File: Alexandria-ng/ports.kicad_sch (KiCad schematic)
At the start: 56 parts, among them J1 Eth0, J10 PoE3, J11 PoE4, J12 FFC, J2 Eth1, J3 Eth2, J4 Eth3, J5 Eth4, J6 SFP+, J7 PoE0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

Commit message: Update to KiCad 7.0, add footprint to RJ45 jacks
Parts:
- J1, J2, J3, J4, J5: footprint (none) -> Connector_RJ:RJ45_Amphenol_RJHSE538X
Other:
- note added: "DS1128: Footprint matches Amphenol RJHSE538X"

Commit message: Annotate & assign footprints
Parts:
- D3, D4, D5: footprint (none) -> LED_SMD:LED_0603_1608Metric_Pad1.05x0.95mm_HandSolder
- J6: footprint (none) -> Connector:Connector_SFP_and_Cage
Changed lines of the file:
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@@
       (effects (font (size 1.27 1.27)) (justify right))
     )
-    (property "Footprint" "" (at 217.17 41.91 0)
+    (property "Footprint" "LED_SMD:LED_0603_1608Metric_Pad1.05x0.95mm_HandSolder" (at 217.17 41.91 0)
       (effects (font (size 1.27 1.27)) hide)
     )
@@
       (effects (font (size 1.27 1.27)) (justify right))
     )
-    (property "Footprint" "" (at 271.78 35.56 0)
+    (property "Footprint" "LED_SMD:LED_0603_1608Metric_Pad1.05x0.95mm_HandSolder" (at 271.78 35.56 0)
       (effects (font (size 1.27 1.27)) hide)
     )
@@
       (effects (font (size 1.27 1.27)) (justify right))
     )
-    (property "Footprint" "" (at 278.13 53.34 0)
+    (property "Footprint" "LED_SMD:LED_0603_1608Metric_Pad1.05x0.95mm_HandSolder" (at 278.13 53.34 0)
       (effects (font (size 1.27 1.27)) hide)
     )
@@
       (effects (font (size 1.27 1.27)) (justify left))
     )
-    (property "Footprint" "" (at 248.92 60.96 0)
-      (effects (font (size 1.27 1.27)) hide)
-    )
+    (property "Footprint" "Connector:Connector_SFP_and_Cage" (at 248.92 60.96 0)
+      (effects (font (size 1.27 1.27)) hide)
+    )

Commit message: Add IRQ test point & SFP I2C header
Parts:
- added J14: I²C, Connector_PinHeader_2.54mm:PinHeader_1x02_P2.54mm_Vertical, symbol Connector_Generic:Conn_01x02
- added TP1: IRQ, TestPoint:TestPoint_Pad_D1.0mm, symbol Connector:TestPoint
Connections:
- net at J6.5 (SCL), R48.1: now also J14.2 (Pin_2)
- net at J6.4 (SDA), R50.1: now also J14.1 (Pin_1)
- new net IRQ: TP1.1
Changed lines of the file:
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@@
   (junction (at 199.39 130.81) (diameter 0) (color 0 0 0 0)
   )
+  (junction (at 232.41 31.75) (diameter 0) (color 0 0 0 0)
+  )
   (junction (at 161.29 130.81) (diameter 0) (color 0 0 0 0)
   )
   (junction (at 217.17 36.83) (diameter 0) (color 0 0 0 0)
   )
+  (junction (at 227.33 34.29) (diameter 0) (color 0 0 0 0)
+  )
   (junction (at 199.39 95.25) (diameter 0) (color 0 0 0 0)
   )
@@
     (stroke (width 0) (type default))
   )
-  (wire (pts (xy 224.79 34.29) (xy 236.22 34.29))
+  (wire (pts (xy 224.79 34.29) (xy 227.33 34.29))
     (stroke (width 0) (type default))
   )
@@
     (stroke (width 0) (type default))
   )
+  (wire (pts (xy 229.87 31.75) (xy 232.41 31.75))
+    (stroke (width 0) (type default))
+  )
   (wire (pts (xy 111.76 24.13) (xy 106.68 24.13))
     (stroke (width 0) (type default))
@@
     (stroke (width 0) (type default))
   )
+  (wire (pts (xy 227.33 34.29) (xy 227.33 38.1))
+    (stroke (width 0) (type default))
+  )
   (wire (pts (xy 199.39 59.69) (xy 191.77 59.69))
     (stroke (width 0) (type default))
@@
     (stroke (width 0) (type default))
   )
+  (wire (pts (xy 229.87 38.1) (xy 229.87 31.75))
+    (stroke (width 0) (type default))
+  )
   (wire (pts (xy 96.52 87.63) (xy 99.06 87.63))
     (stroke (width 0) (type default))
@@
     (stroke (width 0) (type default))
   )
+  (wire (pts (xy 227.33 34.29) (xy 236.22 34.29))
+    (stroke (width 0) (type default))
+  )
   (wire (pts (xy 231.14 54.61) (xy 231.14 57.15))
     (stroke (width 0) (type default))
@@
     )
   )
+  (global_label "IRQ" (shape input) (at 241.3 73.66 270) (fields_autoplaced)
+    (effects (font (size 1.27 1.27)) (justify right))
+    (property "Intersheetrefs" "${INTERSHEET_REFS}" (at 241.3 79.7711 90)
+      (effects (font (size 1.27 1.27)) (justify right) hide)
+    )
+  )
   (global_label "P1BP" (shape input) (at 49.53 57.15 90) (fields_autoplaced)
     (effects (font (size 1.27 1.27)) (justify left))
@@
     )
   )
+  (symbol (lib_id "Connector_Generic:Conn_01x02") (at 229.87 43.18 270) (unit 1)
+    (in_bom yes) (on_board yes) (dnp no)
+    (property "Reference" "J14" (at 226.06 45.72 90)
+      (effects (font (size 1.27 1.27)) (justify left))
+    )
+    (property "Value" "I²C" (at 226.06 48.26 90)
+      (effects (font (size 1.27 1.27)) (justify left))
+    )
+    (property "Footprint" "Connector_PinHeader_2.54mm:PinHeader_1x02_P2.54mm_Vertical" (at 229.87 43.18 0)
+      (effects (font (size 1.27 1.27)) hide)
+    )
+    (property "Datasheet" "~" (at 229.87 43.18 0)
+      (effects (font (size 1.27 1.27)) hide)
+    )
+    (pin "1")
+    (pin "2")
+    (instances
+      (project "Alexandria-ng"
+        (path "/d75cf6f5-5ddc-4328-8d5c-12d6ef92ffe7/775fe030-611a-432c-a4dd-ed09d01a918c"
+          (reference "J14") (unit 1)
+        )
+      )
+    )
+  )
   (symbol (lib_id "Device:R") (at 184.15 99.06 180) (unit 1)
     (in_bom yes) (on_board yes) (dnp no) (fields_autoplaced)
@@
         )
       )
+    )
+  )
+  (symbol (lib_id "Connector:TestPoint") (at 241.3 73.66 0) (unit 1)
+    (in_bom yes) (on_board yes) (dnp no) (fields_autoplaced)
+    (property "Reference" "TP1" (at 243.84 69.723 0)
+      (effects (font (size 1.27 1.27)) (justify left))
+    )
+    (property "Value" "IRQ" (at 243.84 72.263 0)
+      (effects (font (size 1.27 1.27)) (justify left))
+    )
+    (property "Footprint" "TestPoint:TestPoint_Pad_D1.0mm" (at 246.38 73.66 0)
+      (effects (font (size 1.27 1.27)) hide)
+    )
+    (property "Datasheet" "~" (at 246.38 73.66 0)
+      (effects (font (size 1.27 1.27)) hide)
+    )
+    (pin "1")
+    (instances
+      (project "Alexandria-ng"
+        (path "/d75cf6f5-5ddc-4328-8d5c-12d6ef92ffe7/775fe030-611a-432c-a4dd-ed09d01a918c"
+          (reference "TP1") (unit 1)
+        )
+      )

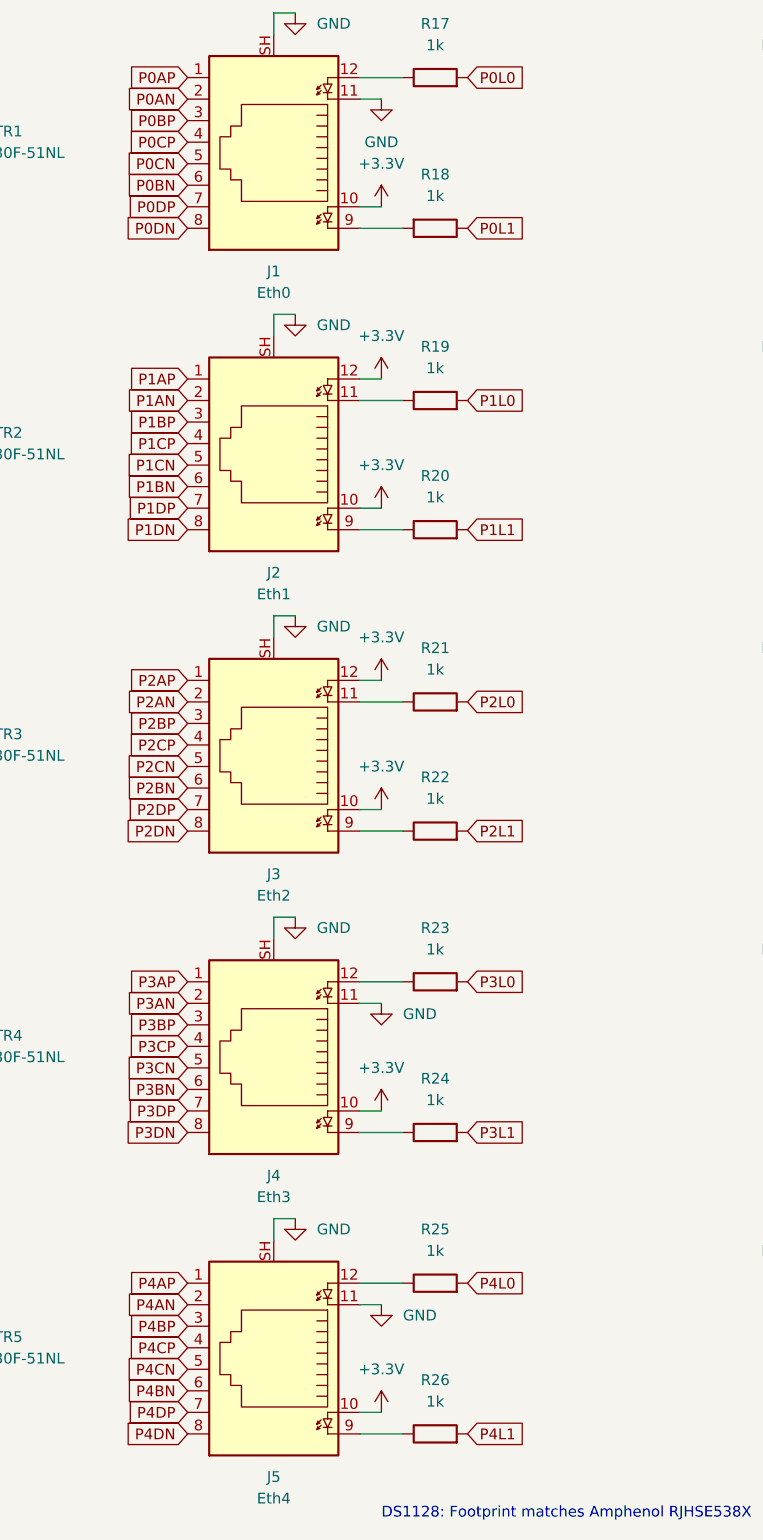
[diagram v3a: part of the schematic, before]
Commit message: Switch DVDDIO pins to +2.8V
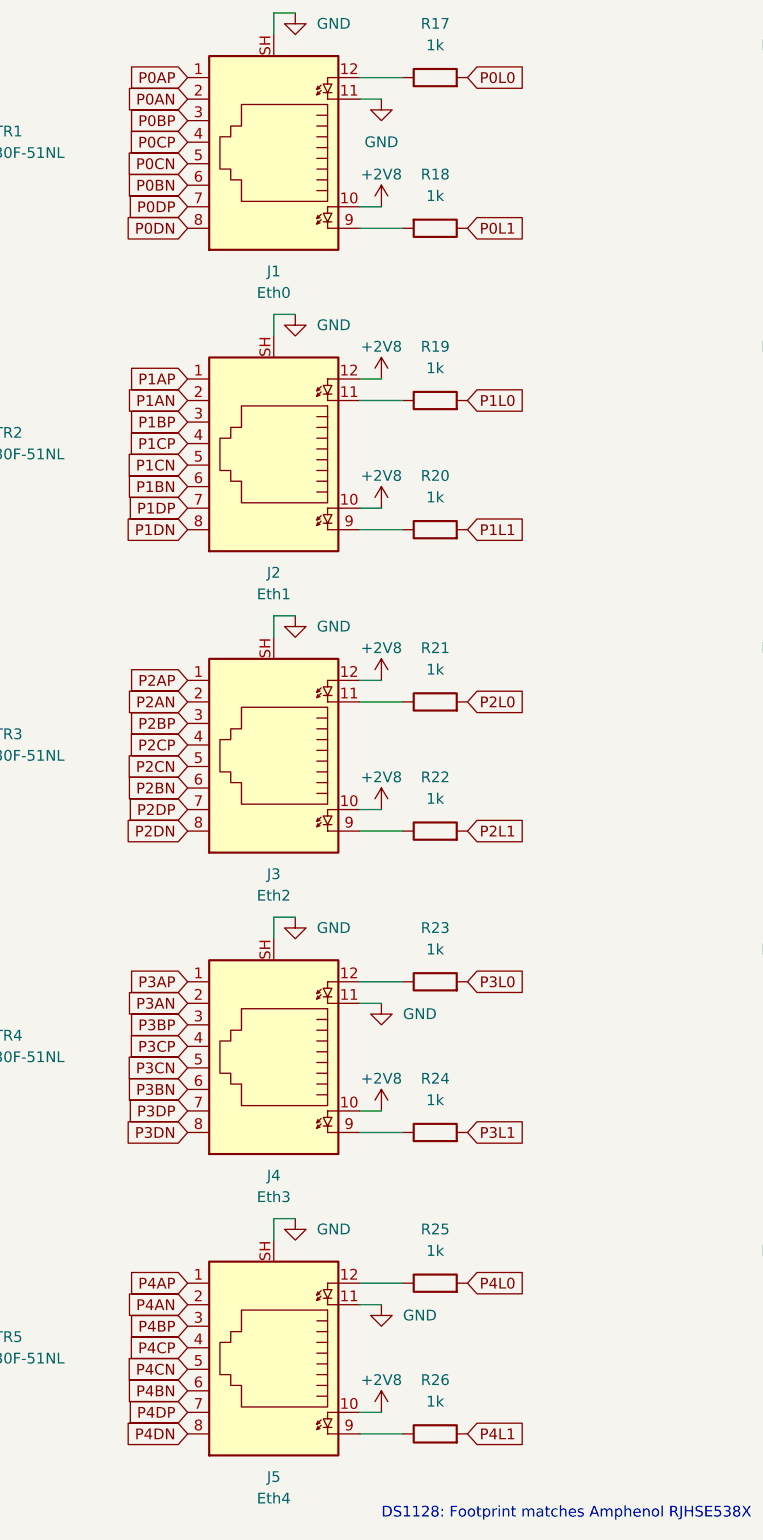
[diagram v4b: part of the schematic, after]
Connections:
- net +2V8: now also J1.10, J2.10, J2.12, J3.10, J3.12, J4.10, J5.10
- net +3.3V: no longer J1.10, J2.10, J2.12, J3.10, J3.12, J4.10, J5.10
